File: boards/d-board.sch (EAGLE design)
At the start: 32 parts, among them J1 AMP FCI 10103594-0001LF, U1 ESP-WROOM-32, U2 CP2104, U3 SP0503BAHT

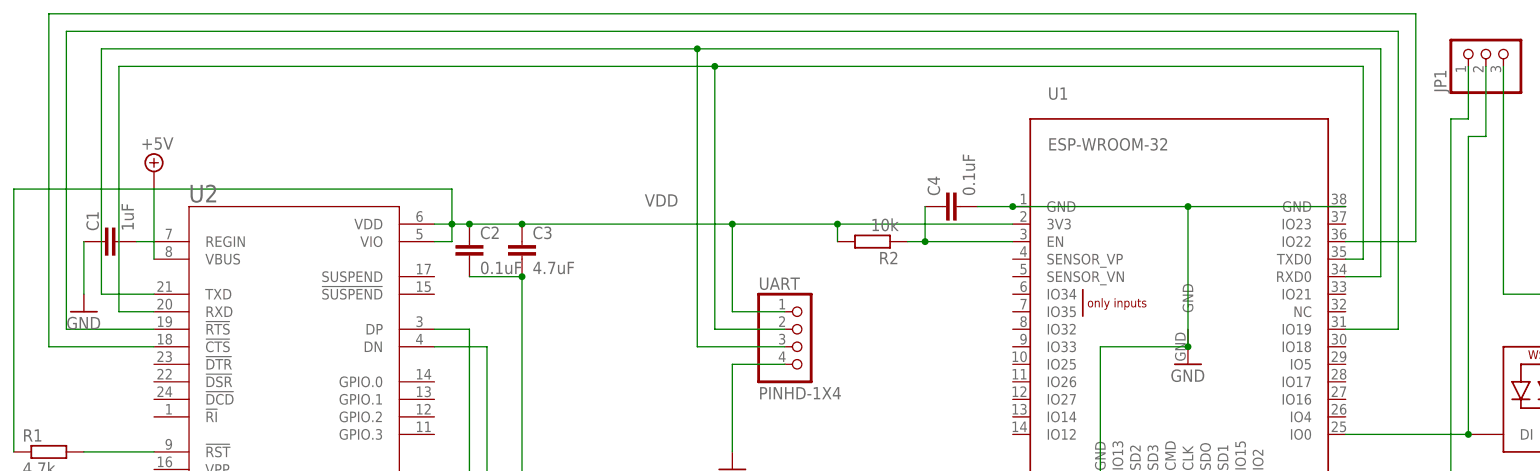
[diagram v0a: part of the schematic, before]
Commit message: Update board to rev.2
Fixes CP2104 REGIN not connected to +5V.

Replaces the mis-pinned 3535 neopixel with the 5050 part that is correct instead.
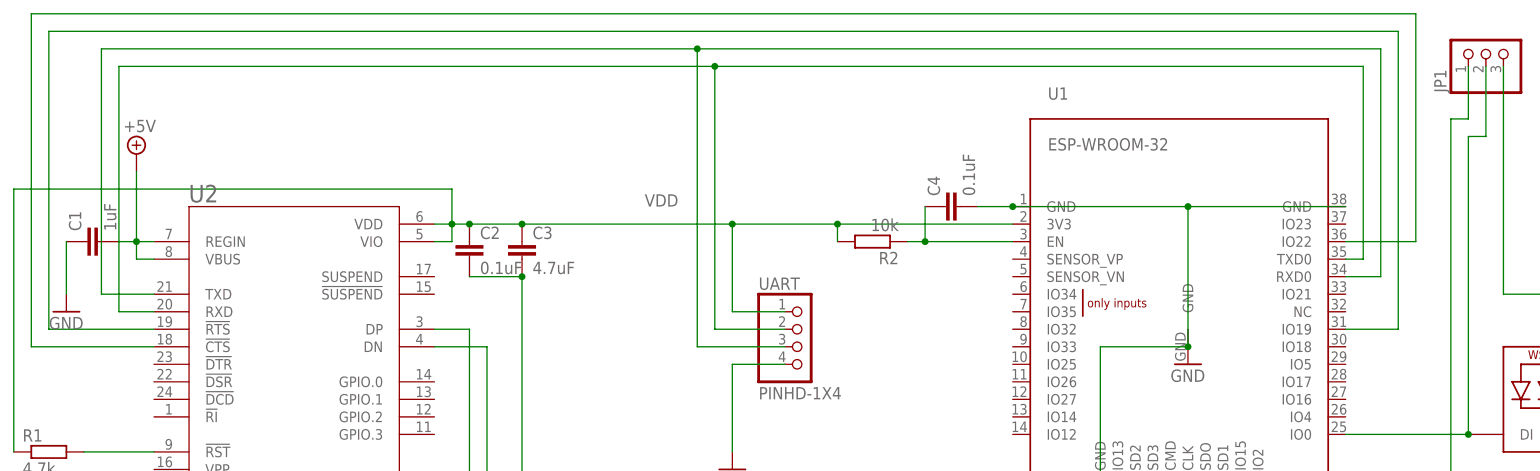
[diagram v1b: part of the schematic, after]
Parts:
- LED1, LED10, LED2, LED3, LED4, LED5, LED6, LED7, LED8, LED9: value WS2812B3535 -> WS2812B5050; device adafruit:WS2812B3535 -> adafruit:WS2812B5050
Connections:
- removed net N$15: C1.2, U2.REGIN
- net +5V: now also C1.2, U2.REGIN
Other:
- moved on the sheet: C1
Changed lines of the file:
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@@
 <part name="SUPPLY1" library="supply2" library_urn="urn:adsk.eagle:library:372" deviceset="+5V" device=""/>
 <part name="SUPPLY2" library="supply2" library_urn="urn:adsk.eagle:library:372" deviceset="+5V" device=""/>
-<part name="LED1" library="adafruit" library_urn="urn:adsk.eagle:library:420" deviceset="WS2812B" device="3535" package3d_urn="urn:adsk.eagle:package:6240962/1"/>
-<part name="LED2" library="adafruit" library_urn="urn:adsk.eagle:library:420" deviceset="WS2812B" device="3535" package3d_urn="urn:adsk.eagle:package:6240962/1"/>
-<part name="LED3" library="adafruit" library_urn="urn:adsk.eagle:library:420" deviceset="WS2812B" device="3535" package3d_urn="urn:adsk.eagle:package:6240962/1"/>
-<part name="LED4" library="adafruit" library_urn="urn:adsk.eagle:library:420" deviceset="WS2812B" device="3535" package3d_urn="urn:adsk.eagle:package:6240962/1"/>
-<part name="LED5" library="adafruit" library_urn="urn:adsk.eagle:library:420" deviceset="WS2812B" device="3535" package3d_urn="urn:adsk.eagle:package:6240962/1"/>
-<part name="LED6" library="adafruit" library_urn="urn:adsk.eagle:library:420" deviceset="WS2812B" device="3535" package3d_urn="urn:adsk.eagle:package:6240962/1"/>
-<part name="LED7" library="adafruit" library_urn="urn:adsk.eagle:library:420" deviceset="WS2812B" device="3535" package3d_urn="urn:adsk.eagle:package:6240962/1"/>
-<part name="LED8" library="adafruit" library_urn="urn:adsk.eagle:library:420" deviceset="WS2812B" device="3535" package3d_urn="urn:adsk.eagle:package:6240962/1"/>
-<part name="LED9" library="adafruit" library_urn="urn:adsk.eagle:library:420" deviceset="WS2812B" device="3535" package3d_urn="urn:adsk.eagle:package:6240962/1"/>
-<part name="LED10" library="adafruit" library_urn="urn:adsk.eagle:library:420" deviceset="WS2812B" device="3535" package3d_urn="urn:adsk.eagle:package:6240962/1"/>
+<part name="LED1" library="adafruit" deviceset="WS2812B" device="5050" value="WS2812B5050"/>
+<part name="LED2" library="adafruit" deviceset="WS2812B" device="5050" value="WS2812B5050"/>
+<part name="LED3" library="adafruit" deviceset="WS2812B" device="5050" value="WS2812B5050"/>
+<part name="LED4" library="adafruit" deviceset="WS2812B" device="5050" value="WS2812B5050"/>
+<part name="LED5" library="adafruit" deviceset="WS2812B" device="5050" value="WS2812B5050"/>
+<part name="LED6" library="adafruit" deviceset="WS2812B" device="5050" value="WS2812B5050"/>
+<part name="LED7" library="adafruit" deviceset="WS2812B" device="5050" value="WS2812B5050"/>
+<part name="LED8" library="adafruit" deviceset="WS2812B" device="5050" value="WS2812B5050"/>
+<part name="LED9" library="adafruit" deviceset="WS2812B" device="5050" value="WS2812B5050"/>
+<part name="LED10" library="adafruit" deviceset="WS2812B" device="5050" value="WS2812B5050"/>
 <part name="GND2" library="supply1" library_urn="urn:adsk.eagle:library:371" deviceset="GND" device=""/>
 <part name="SUPPLY3" library="supply2" library_urn="urn:adsk.eagle:library:372" deviceset="+5V" device=""/>
@@
 <attribute name="VALUE" x="-21.59" y="17.018" size="1.778" layer="96"/>
 </instance>
-<instance part="C1" gate="G$1" x="-10.16" y="50.8" smashed="yes" rot="R90">
-<attribute name="NAME" x="-10.541" y="52.324" size="1.778" layer="95" rot="R90"/>
-<attribute name="VALUE" x="-5.461" y="52.324" size="1.778" layer="96" rot="R90"/>
+<instance part="C1" gate="G$1" x="-12.7" y="50.8" smashed="yes" rot="R90">
+<attribute name="NAME" x="-13.081" y="52.324" size="1.778" layer="95" rot="R90"/>
+<attribute name="VALUE" x="-8.001" y="52.324" size="1.778" layer="96" rot="R90"/>
 </instance>
 <instance part="U3" gate="G$1" x="58.42" y="-15.24" smashed="yes" rot="R90" grouprefs="USB_PORT">
@@
 <attribute name="VALUE" x="58.42" y="-38.1" size="1.778" layer="96"/>
 </instance>
-<instance part="GND5" gate="1" x="-12.7" y="40.64" smashed="yes">
-<attribute name="VALUE" x="-15.24" y="38.1" size="1.778" layer="96"/>
+<instance part="GND5" gate="1" x="-15.24" y="40.64" smashed="yes">
+<attribute name="VALUE" x="-17.78" y="38.1" size="1.778" layer="96"/>
 </instance>
 <instance part="C2" gate="G$1" x="43.18" y="50.8" smashed="yes">
@@
 <attribute name="VALUE" x="31.115" y="-6.985" size="1.778" layer="96"/>
 </instance>
-<instance part="SUPPLY2" gate="+5V" x="-2.54" y="60.96" smashed="yes">
-<attribute name="VALUE" x="-4.445" y="64.135" size="1.778" layer="96"/>
+<instance part="SUPPLY2" gate="+5V" x="-5.08" y="63.5" smashed="yes">
+<attribute name="VALUE" x="-6.985" y="66.675" size="1.778" layer="96"/>
 </instance>
 <instance part="LED1" gate="G$1" x="200.66" y="25.4" smashed="yes"/>
@@
 <pinref part="GND5" gate="1" pin="GND"/>
 <pinref part="C1" gate="G$1" pin="1"/>
-<wire x1="-12.7" y1="43.18" x2="-12.7" y2="50.8" width="0.1524" layer="91"/>
+<wire x1="-15.24" y1="43.18" x2="-15.24" y2="50.8" width="0.1524" layer="91"/>
 </segment>
 <segment>
@@
 <pinref part="SUPPLY2" gate="+5V" pin="+5V"/>
 <pinref part="U2" gate="IC" pin="VBUS"/>
-<wire x1="-2.54" y1="58.42" x2="-2.54" y2="48.26" width="0.1524" layer="91"/>
+<wire x1="-5.08" y1="60.96" x2="-5.08" y2="50.8" width="0.1524" layer="91"/>
+<pinref part="C1" gate="G$1" pin="2"/>
+<pinref part="U2" gate="IC" pin="REGIN"/>
+<wire x1="-2.54" y1="50.8" x2="-5.08" y2="50.8" width="0.1524" layer="91"/>
+<wire x1="-5.08" y1="50.8" x2="-7.62" y2="50.8" width="0.1524" layer="91"/>
+<wire x1="-2.54" y1="48.26" x2="-5.08" y2="48.26" width="0.1524" layer="91"/>
+<wire x1="-5.08" y1="48.26" x2="-5.08" y2="50.8" width="0.1524" layer="91"/>
+<junction x="-5.08" y="50.8"/>
 </segment>
 <segment>
@@
 <wire x1="170.18" y1="38.1" x2="177.8" y2="38.1" width="0.1524" layer="91"/>
 <wire x1="177.8" y1="38.1" x2="177.8" y2="81.28" width="0.1524" layer="91"/>
-<wire x1="177.8" y1="81.28" x2="-15.24" y2="81.28" width="0.1524" layer="91"/>
+<wire x1="177.8" y1="81.28" x2="-17.78" y2="81.28" width="0.1524" layer="91"/>
 <pinref part="U2" gate="IC" pin="!RTS"/>
-<wire x1="-15.24" y1="81.28" x2="-15.24" y2="38.1" width="0.1524" layer="91"/>
-<wire x1="-15.24" y1="38.1" x2="-2.54" y2="38.1" width="0.1524" layer="91"/>
+<wire x1="-17.78" y1="81.28" x2="-17.78" y2="38.1" width="0.1524" layer="91"/>
+<wire x1="-17.78" y1="38.1" x2="-2.54" y2="38.1" width="0.1524" layer="91"/>
 </segment>
 </net>
@@
 <wire x1="170.18" y1="50.8" x2="180.34" y2="50.8" width="0.1524" layer="91"/>
 <wire x1="180.34" y1="50.8" x2="180.34" y2="83.82" width="0.1524" layer="91"/>
-<wire x1="180.34" y1="83.82" x2="-17.78" y2="83.82" width="0.1524" layer="91"/>
+<wire x1="180.34" y1="83.82" x2="-20.32" y2="83.82" width="0.1524" layer="91"/>
 <pinref part="U2" gate="IC" pin="!CTS"/>
-<wire x1="-17.78" y1="83.82" x2="-17.78" y2="35.56" width="0.1524" layer="91"/>
-<wire x1="-17.78" y1="35.56" x2="-2.54" y2="35.56" width="0.1524" layer="91"/>
-</segment>
-</net>
-<net name="N$15" class="0">
-<segment>
-<pinref part="C1" gate="G$1" pin="2"/>
-<pinref part="U2" gate="IC" pin="REGIN"/>
-<wire x1="-2.54" y1="50.8" x2="-5.08" y2="50.8" width="0.1524" layer="91"/>
-</segment>
-</net>
+<wire x1="-20.32" y1="83.82" x2="-20.32" y2="35.56" width="0.1524" layer="91"/>
+<wire x1="-20.32" y1="35.56" x2="-2.54" y2="35.56" width="0.1524" layer="91"/>
+</segment>
+</net>

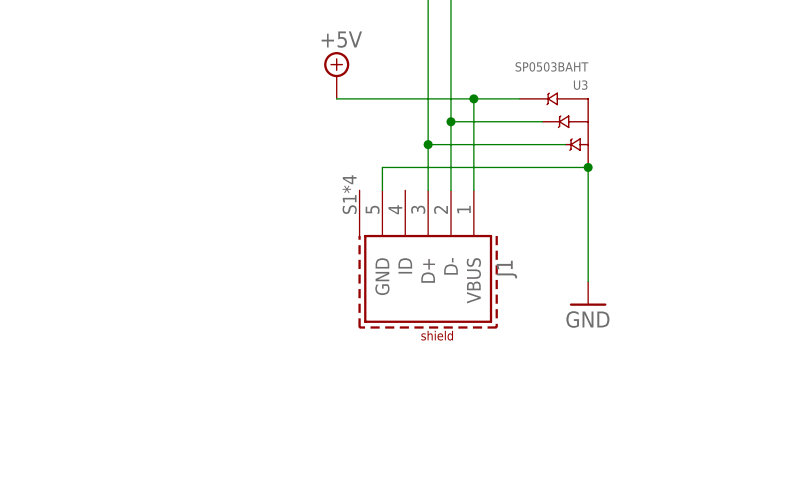
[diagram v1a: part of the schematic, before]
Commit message: Replace the microUSB connector.
Instead of the Wurth part that seems to be harder to find, use a SnapEDA for an Amphenol 10103594-0001LF connector that appears easier to source.
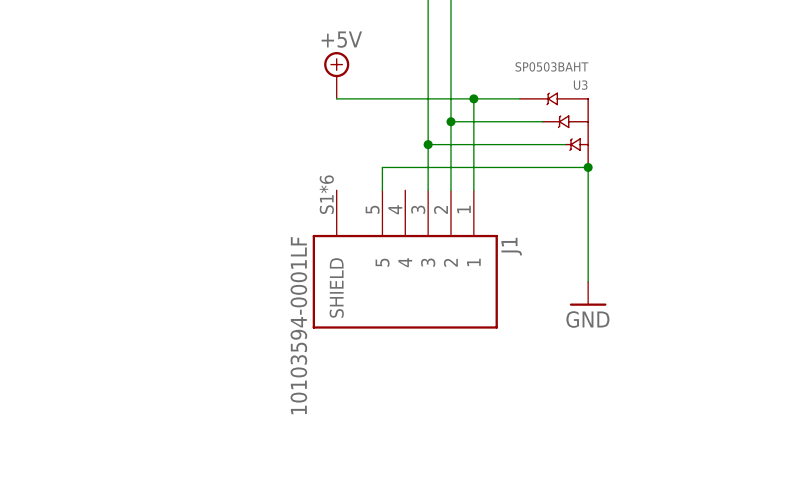
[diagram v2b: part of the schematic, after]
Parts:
- J1: value AMP FCI 10103594-0001LF -> 10103594-0001LF; device Wurth_Connectors_WR-USB:629105150521 -> 10103594-0001LF:10103594-0001LF
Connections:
- net +5V: now also J1.1; no longer J1.VBUS
- net GND: now also J1.5; no longer J1.GND
- net N$6: now also J1.3; no longer J1.D+
- net N$7: now also J1.2; no longer J1.D-
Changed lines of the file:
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@@
 <part name="U2" library="CP2104" deviceset="CP2104" device="-F03-GM" value="CP2104"/>
 <part name="GND1" library="supply1" library_urn="urn:adsk.eagle:library:371" deviceset="GND" device=""/>
-<part name="J1" library="Wurth_Connectors_WR-USB" library_urn="urn:adsk.eagle:library:16513831" deviceset="629105150521" device="" package3d_urn="urn:adsk.eagle:package:16513895/2" value="AMP FCI 10103594-0001LF"/>
 <part name="GND3" library="supply1" library_urn="urn:adsk.eagle:library:371" deviceset="GND" device=""/>
 <part name="R1" library="rcl" library_urn="urn:adsk.eagle:library:334" deviceset="R-EU_" device="R0805" package3d_urn="urn:adsk.eagle:package:23553/2" value="4.7k"/>
@@
 <part name="UART" library="Connector" library_urn="urn:adsk.eagle:library:16378166" deviceset="PINHD-1X4" device="" package3d_urn="urn:adsk.eagle:package:22407/2"/>
 <part name="GND6" library="supply1" library_urn="urn:adsk.eagle:library:371" deviceset="GND" device=""/>
+<part name="J1" library="10103594-0001LF" deviceset="10103594-0001LF" device=""/>
 </parts>
 <sheets>
@@
 <instance part="GND1" gate="1" x="50.8" y="7.62" smashed="yes">
 <attribute name="VALUE" x="48.26" y="5.08" size="1.778" layer="96"/>
-</instance>
-<instance part="J1" gate="G$1" x="43.18" y="-33.02" smashed="yes" rot="R270" grouprefs="USB_PORT">
-<attribute name="NAME" x="50.8" y="-30.48" size="1.778" layer="95" font="vector" rot="R270"/>
 </instance>
 <instance part="GND3" gate="1" x="147.32" y="33.02" smashed="yes">
@@
 <instance part="GND6" gate="1" x="81.28" y="17.78" smashed="yes">
 <attribute name="VALUE" x="78.74" y="15.24" size="1.778" layer="96"/>
+</instance>
+<instance part="J1" gate="G$1" x="40.64" y="-33.02" smashed="yes" rot="R270" grouprefs="USB_PORT">
+<attribute name="NAME" x="51.3259" y="-27.92928125" size="1.7805" layer="95" rot="R270"/>
+<attribute name="VALUE" x="27.9243" y="-27.933259375" size="1.77956875" layer="96" rot="R270"/>
 </instance>
 </instances>
@@
 <pinref part="GND4" gate="1" pin="GND"/>
 <wire x1="60.96" y1="-33.02" x2="60.96" y2="-20.32" width="0.1524" layer="91" grouprefs="USB_PORT"/>
-<pinref part="J1" gate="G$1" pin="GND"/>
 <wire x1="38.1" y1="-22.86" x2="38.1" y2="-20.32" width="0.1524" layer="91" grouprefs="USB_PORT"/>
 <wire x1="38.1" y1="-20.32" x2="60.96" y2="-20.32" width="0.1524" layer="91" grouprefs="USB_PORT"/>
 <junction x="60.96" y="-20.32" grouprefs="USB_PORT"/>
+<pinref part="J1" gate="G$1" pin="5"/>
 </segment>
 <segment>
@@
 <net name="+5V" class="1">
 <segment>
-<pinref part="J1" gate="G$1" pin="VBUS"/>
 <wire x1="48.26" y1="-22.86" x2="48.26" y2="-12.7" width="0.1524" layer="91" grouprefs="USB_PORT"/>
 <wire x1="48.26" y1="-12.7" x2="33.02" y2="-12.7" width="0.1524" layer="91" grouprefs="USB_PORT"/>
@@
 <junction x="48.26" y="-12.7" grouprefs="USB_PORT"/>
 <pinref part="SUPPLY1" gate="+5V" pin="+5V"/>
+<pinref part="J1" gate="G$1" pin="1"/>
 </segment>
 <segment>
@@
 <net name="N$6" class="0">
 <segment>
-<pinref part="J1" gate="G$1" pin="D+"/>
 <wire x1="43.18" y1="-22.86" x2="43.18" y2="-17.78" width="0.1524" layer="91" grouprefs="USB_PORT"/>
 <pinref part="U2" gate="IC" pin="DP"/>
@@
 <wire x1="58.42" y1="-17.78" x2="43.18" y2="-17.78" width="0.1524" layer="91" grouprefs="USB_PORT"/>
 <junction x="43.18" y="-17.78" grouprefs="USB_PORT"/>
+<pinref part="J1" gate="G$1" pin="3"/>
 </segment>
 </net>
 <net name="N$7" class="0">
 <segment>
-<pinref part="J1" gate="G$1" pin="D-"/>
 <pinref part="U2" gate="IC" pin="DN"/>
 <wire x1="45.72" y1="-22.86" x2="45.72" y2="-15.24" width="0.1524" layer="91" grouprefs="USB_PORT"/>
@@
 <wire x1="55.88" y1="-15.24" x2="45.72" y2="-15.24" width="0.1524" layer="91" grouprefs="USB_PORT"/>
 <junction x="45.72" y="-15.24" grouprefs="USB_PORT"/>
-</segment>
-</net>
+<pinref part="J1" gate="G$1" pin="2"/>
+</segment>
+</net>

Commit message: Make it possible to program the ESP32 via serial.
This includes RESET and BOOT pushbuttons to control a solder ESP32, and re-wires the RTS/DTR to control the boot mode of the board for compatibility with the esptool command line.
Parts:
- added BOOT, RESET: DTS-3, switch-tact:DTS-3
- JP1: value (none) -> PINHD-1X3/90; device pinhead:PINHD-1X3 -> Connector:PINHD-1X3/90
- UART: value PINHD-1X4 -> PINHD-1X6/90; device Connector:PINHD-1X4 -> Connector:PINHD-1X6/90
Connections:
- removed net N$13: U1.IO19, U2.!RTS
- removed net N$14: U1.IO22, U2.!CTS
- removed net N$2: U1.TXD0, U2.RXD, UART.2
- removed net N$3: U1.RXD0, U2.TXD, UART.3
- removed net N$9: C4.1, R2.1, U1.EN
- new net ESP32_CTS: BOOT.2, U1.IO0, U2.!RTS, UART.1
- new net ESP32_RTS: C4.1, R2.1, RESET.2, U1.EN, U2.!DTR, UART.6
- new net FROM_ESP: U1.TXD0, U2.RXD, UART.3
- new net TO_ESP: U1.RXD0, U2.TXD, UART.4
- net GND: now also BOOT.1, RESET.1, UART.5; no longer UART.4
- net N$1: now also U1.IO16; no longer U1.IO0
- net VDD: now also UART.2; no longer UART.1
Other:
- moved on the sheet: C10, C11, C12, C13, C14, C5, C6, C7, C8, C9

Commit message: Replace the CP2104 with a CP2102
The CP2104 is getting harder to source, the CP2102 is pretty much equivalent, but requires more components.
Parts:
- removed C1: 1uF, rcl:C-EUC0805
- removed U2: CP2104, CP2104:CP2104-F03-GM
- added C15: 0.1uF, rcl:C-EUC0805
- added C16: 4.7uF, rcl:C-EUC0805
- added R3: 22.1k, rcl:R-EU_R0805
- added R4: 47.5k, rcl:R-EU_R0805
- added U4: CP2102N-A01-GQFN28, CP2102N-A01-GQFN28:CP2102N-A01-GQFN28
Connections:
- removed net ESP32_CTS: BOOT.2, U1.IO0, U2.!RTS, UART.1
- removed net ESP32_RTS: C4.1, R2.1, RESET.2, U1.EN, U2.!DTR, UART.6
- removed net N$6: J1.3, U2.DP, U3.A
- removed net N$7: J1.2, U2.DN, U3.B
- removed net VDD: C2.1, C3.1, R1.1, R2.2, U1.3V3, U2.VDD, U2.VIO, UART.2
- new net 3V3: C15.1, C16.1, R1.1, R2.2, U1.3V3, U4.VDD, UART.2
- new net D+: J1.3, U3.A, U4.D+
- new net D-: J1.2, U3.B, U4.D-
- new net ESP32_BOOT: BOOT.2, U1.IO0, U4.DTR, UART.1
- new net ESP32_EN: C4.1, R2.1, RESET.2, U1.EN, U4.RTS, UART.6
- new net N$3: R3.1, R4.2, U4.VBUS
- net +5V: now also C2.1, C3.1, R3.2, U4.VREGIN; no longer C1.2, U2.REGIN, U2.VBUS
- net FROM_ESP: now also U4.RXD; no longer U2.RXD
- net GND: now also C15.2, C16.2, R4.1, U4.GND; no longer C1.1, U2.GND
- net N$5: now also U4.!RST; no longer U2.!RST!
- net TO_ESP: now also U4.TXD; no longer U2.TXD
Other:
- moved on the sheet: BOOT, C10, C11, C12, C13, C14, C2, C3, C4, C5, C6, C7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

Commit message: Use net names instead of very long connections.
This allows an easier read of the diagram.
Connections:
- net ESP32_BOOT renamed ESP_BOOT
- net ESP32_EN renamed ESP_EN
- net FROM_ESP renamed ESP_TX
- net N$1 renamed NEOPIXEL_DATA
- net TO_ESP renamed ESP_RX
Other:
- moved on the sheet: BOOT, C10, C11, C12, C13, C14, C15, C16, C2, C3, C4, C5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
